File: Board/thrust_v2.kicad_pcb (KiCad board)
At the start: 2 copper layers, 83.8 x 61 mm, 187 parts, among them J1 Conn_01x05, J10 BattVolt, J12 MX-67068-9000(USB-B), J13 Conn_SWD, J14 Motor, J15 BattCurr, J16 SensorRPM, J17 UART/I2C, J2 Conn_01x05, J3 Conn_01x05, J4 Conn_3.3V, J5 Conn_3.3VA, J7 Conn_01x05, J8 Ext_5V, M1 Mounting_Hole, M2 Mounting_Hole, M3 Mounting_Hole, M4 Mounting_Hole, Q1 MMBT4403, Q2 MMBT4403, Q3 MMBT4403, SW2 BootBtn, SW4 UserBtn, SW5 ResetBtn, U1 NCP1117-3.3/LDI1117-3.3H, U12 STM32F401RETx, U2 MIC5504-3.3YM5, U3 HX711, U4 HX711, U5 HX711, U6 USBLC6-2P6, U7 MCP1501_SOT23, U8 LCD_SSD1306_I2C, Y1 8MHz, Y2 32.768kHz

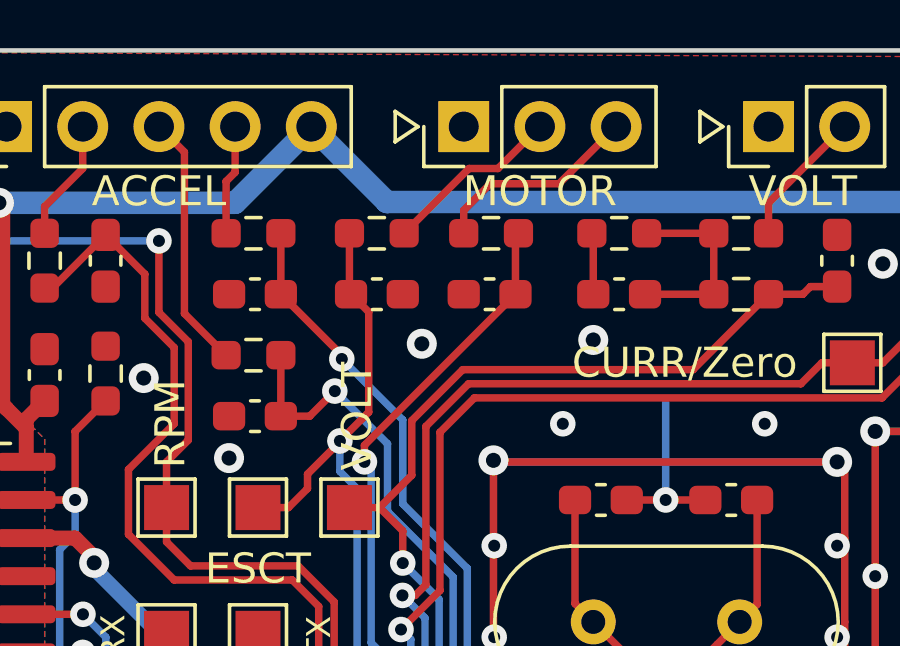
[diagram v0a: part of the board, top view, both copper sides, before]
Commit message: fix curr_zero connection
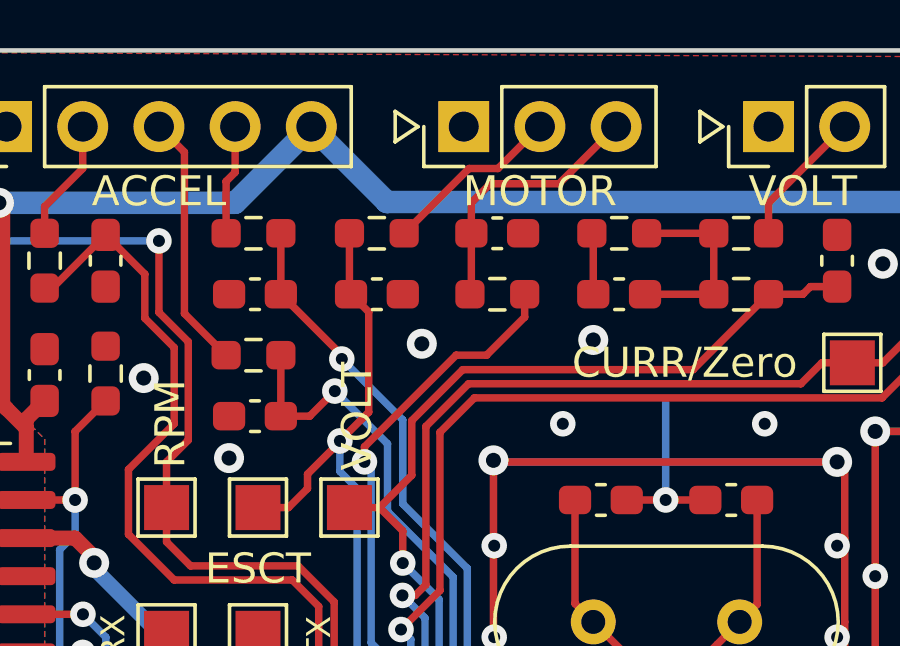
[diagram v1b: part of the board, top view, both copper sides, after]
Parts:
- L4, L5, L7: value f.bead -> f.bead BLM18PG471SH1D
- R41: value 47k -> 8.2k
- R42: value 68k -> 4.7k
- moved C40 2.05 mm to (138.3, 72.1), turned to 0 degrees
- moved R29 2.04 mm to (138.3, 74.2)
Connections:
- C40 pad 1: /MOTOR_OUT -> Net-(C40-Pad1)
- C50 pad 1: /BATT_CURR -> /BATT_CURR_ZERO
- C56 pad 1: /BATT_CURR_ZERO -> /BATT_CURR
- J14 pad 3: Net-(J14-Pad3) -> Net-(C40-Pad1)
- R29 pad 1: Net-(J14-Pad3) -> Net-(C40-Pad1)
- R34 pad 2: /BATT_CURR -> /BATT_CURR_ZERO
- R36 pad 2: /BATT_CURR_ZERO -> /BATT_CURR
- TP17 pad 1: /BATT_CURR -> /BATT_CURR_ZERO
- TP19 pad 1: /BATT_CURR_ZERO -> /BATT_CURR
- U12 pad 20: /BATT_CURR -> /BATT_CURR_ZERO
- U12 pad 21: /BATT_CURR_ZERO -> /BATT_CURR
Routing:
- net Net-(C40-Pad1): track 0.00 -> 8.95 mm
- net Net-(J14-Pad3): track 7.00 -> 0.00 mm
- net /BATT_CURR_ZERO: track 46.9 -> 48.2 mm
- net /BATT_CURR: track 48.2 -> 46.9 mm
- net /MOTOR_OUT: track 40.4 -> 39.1 mm
